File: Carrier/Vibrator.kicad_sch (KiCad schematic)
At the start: 5 parts, among them M1 Z30C1T8460001, Q4 BC847

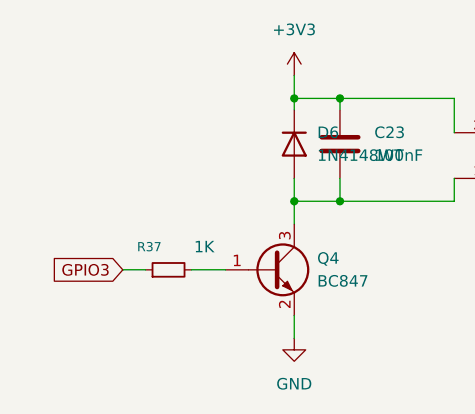
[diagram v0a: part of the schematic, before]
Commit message: fix: sync schematic prot3 and v2.5
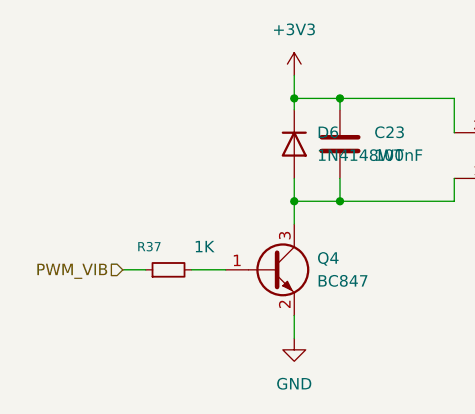
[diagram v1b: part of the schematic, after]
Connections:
- net GPIO3 renamed PWM_VIB
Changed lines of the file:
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@@
 		)
 	)
-	(global_label "GPIO3"
+	(hierarchical_label "PWM_VIB"
 		(shape input)
 		(at 67.31 97.79 180)
-		(fields_autoplaced yes)
 		(effects
 			(font
@@
 			(justify right)
 		)
-		(property "Intersheetrefs" "${INTERSHEET_REFS}"
-			(at 58.64 97.79 0)
-			(effects
-				(font
-					(size 1.27 1.27)
-				)
-				(justify right)
-				(hide yes)
-			)
-		)
 	)

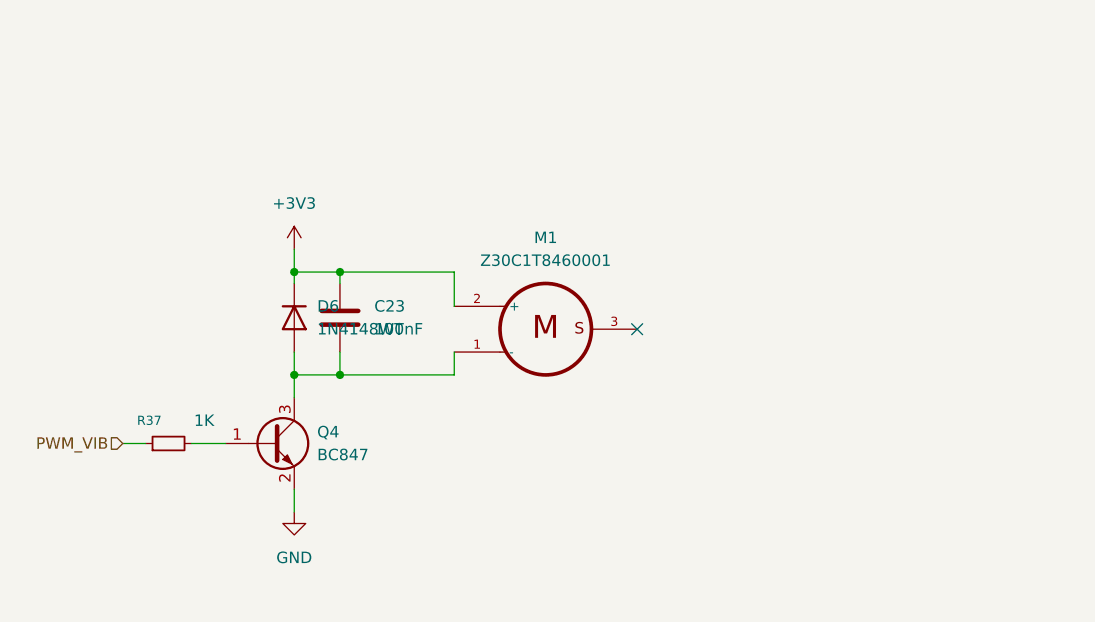
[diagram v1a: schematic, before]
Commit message: schematic update names
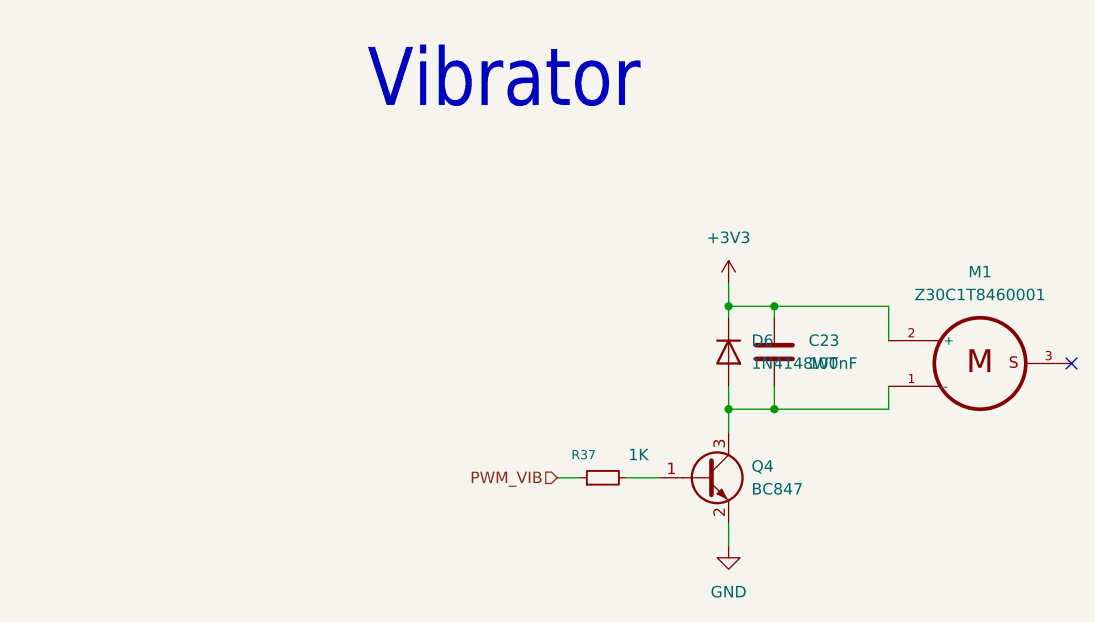
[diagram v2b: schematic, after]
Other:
- note added: "Vibrator"
- moved on the sheet: C23, D6, M1, Q4, R37
